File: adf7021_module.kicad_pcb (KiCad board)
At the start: 4 copper layers, 58 x 26 mm, 70 parts, among them J1 Conn_02x10_Counter_Clockwise, J2 Conn_Coaxial, J3 Conn_Coaxial, J4 Conn_02x10_Counter_Clockwise, J5 Conn_Coaxial, J6 Conn_Coaxial, U1 ADF7021, X1 19.68MHz

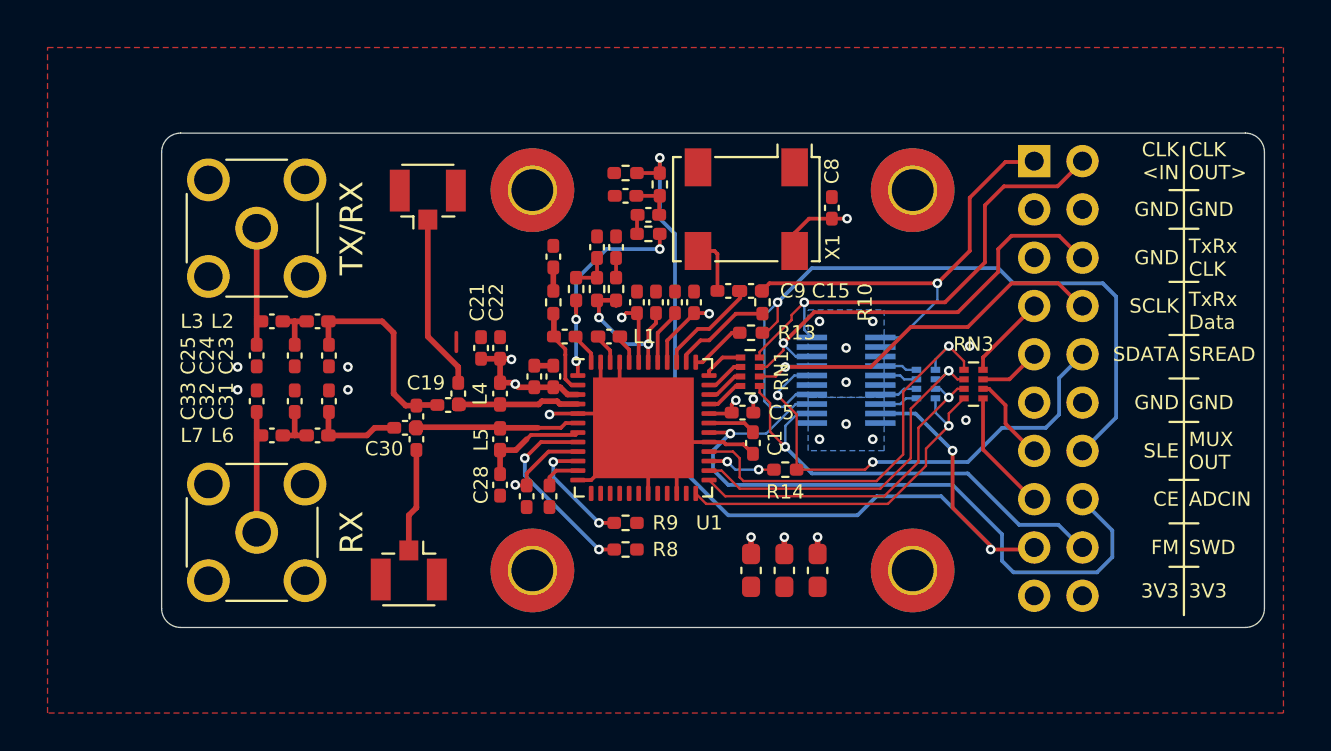
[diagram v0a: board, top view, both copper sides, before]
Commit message: Preliminary via stitching
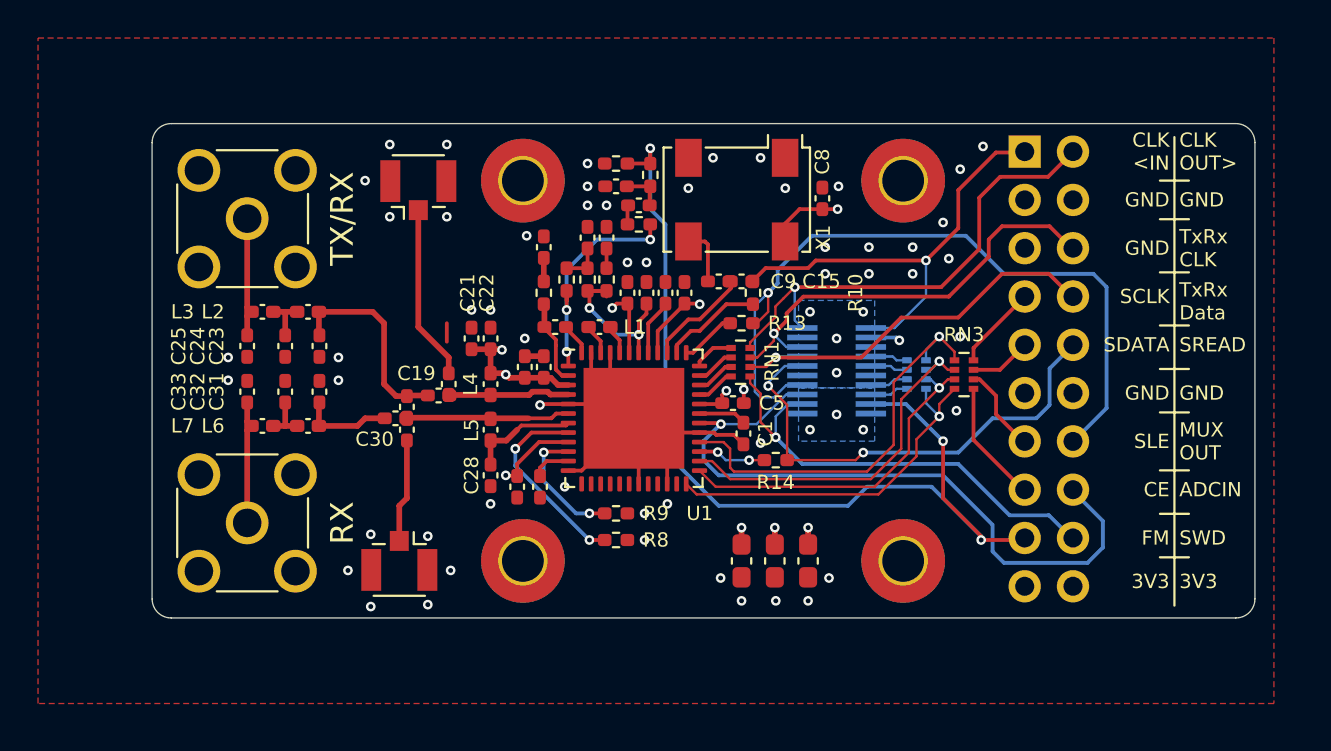
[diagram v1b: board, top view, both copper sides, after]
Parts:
- moved C1 0.71 mm to (136.6, 60.3)
- moved C10 0.71 mm to (131.5, 52.9)
- moved C11 0.71 mm to (129.4, 50.0)
- moved C12 0.71 mm to (128.4, 50.0)
- moved C13 0.71 mm to (126.1, 50.5)
- moved C14 0.71 mm to (132.5, 52.9)
- moved C15 0.71 mm to (136.5, 52.3)
- moved C16 0.71 mm to (131.1, 48.3)
- moved C17 0.71 mm to (129.9, 47.3)
- moved C18 0.71 mm to (121.1, 57.7)
- moved C19 0.71 mm to (120.6, 58.3)
- moved C2 0.71 mm to (133.5, 52.9)
- moved C20 0.71 mm to (124.7, 63.1)
- moved C21 0.71 mm to (122.3, 55.3)
- moved C22 0.71 mm to (123.3, 55.3)
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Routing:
- net GND: track 35.0 -> 36.5 mm, vias 12 -> 60
- net MUXOUT: track 38.5 -> 39.9 mm

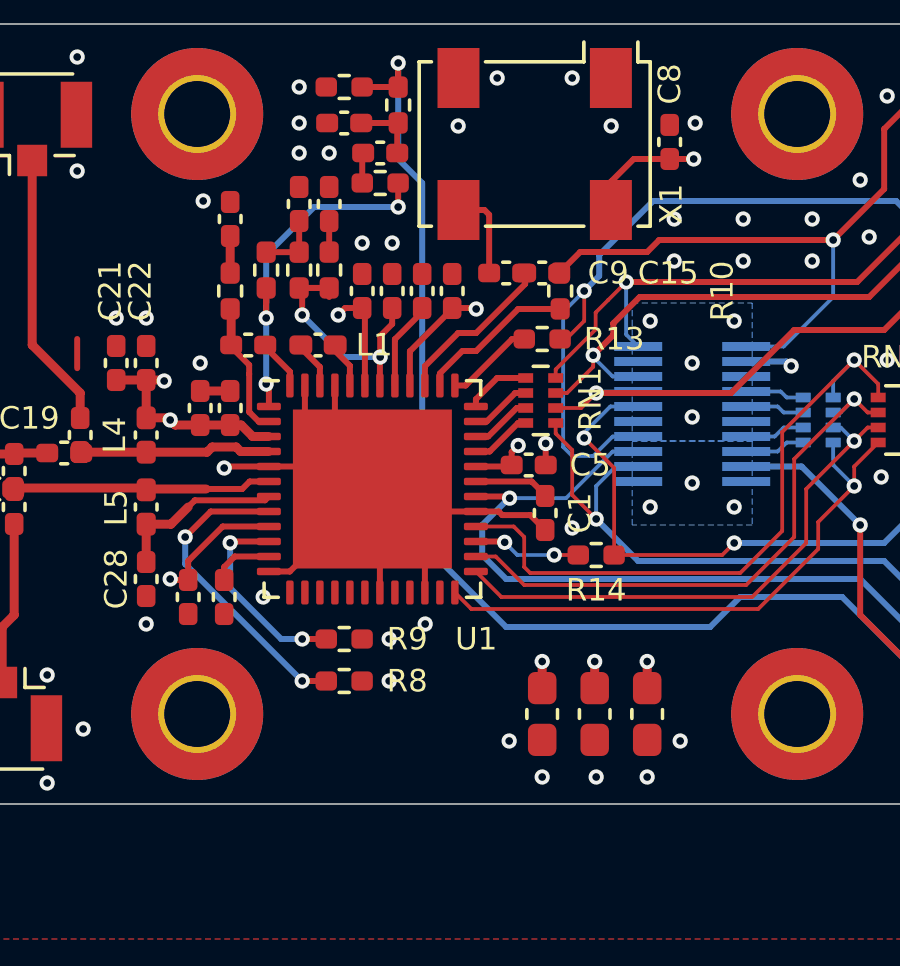
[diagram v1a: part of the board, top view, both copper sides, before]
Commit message: Version silkscreen, via stitching under U1
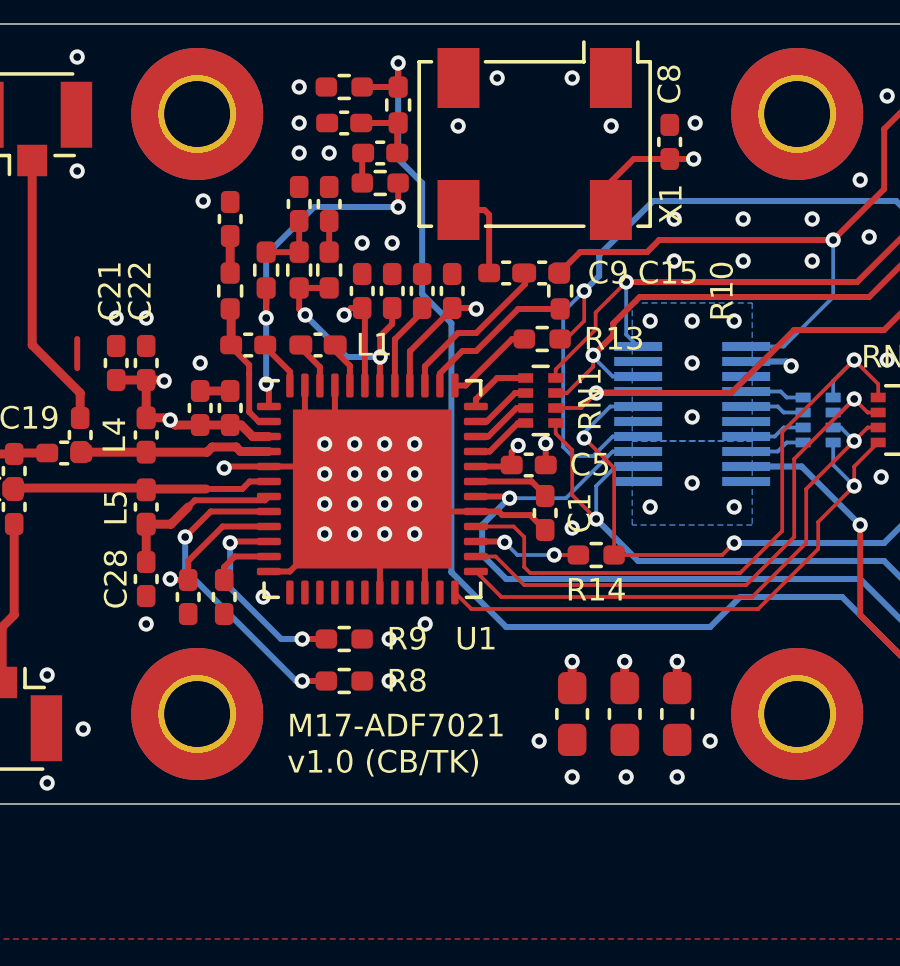
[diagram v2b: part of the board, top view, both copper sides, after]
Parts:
- moved C34 1.00 mm to (141.0, 67.0)
- moved C35 1.00 mm to (139.2, 67.0)
- moved C36 1.00 mm to (137.5, 67.0)
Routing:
- net GND: vias 60 -> 77
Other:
- board text added: "M17-ADF7021 v1.0 (CB/TK)"

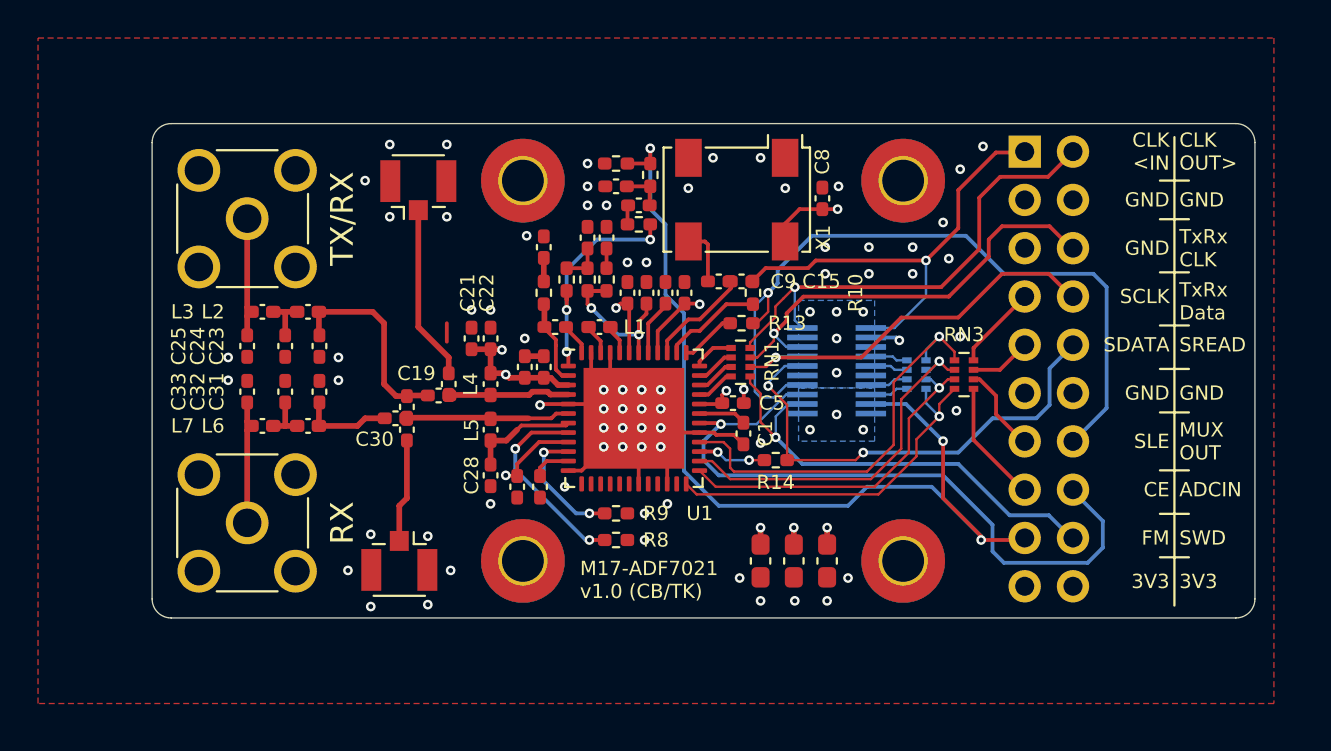
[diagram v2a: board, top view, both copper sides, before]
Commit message: adding shield, moving uFL debug connectors, adding optional SMA clock source input
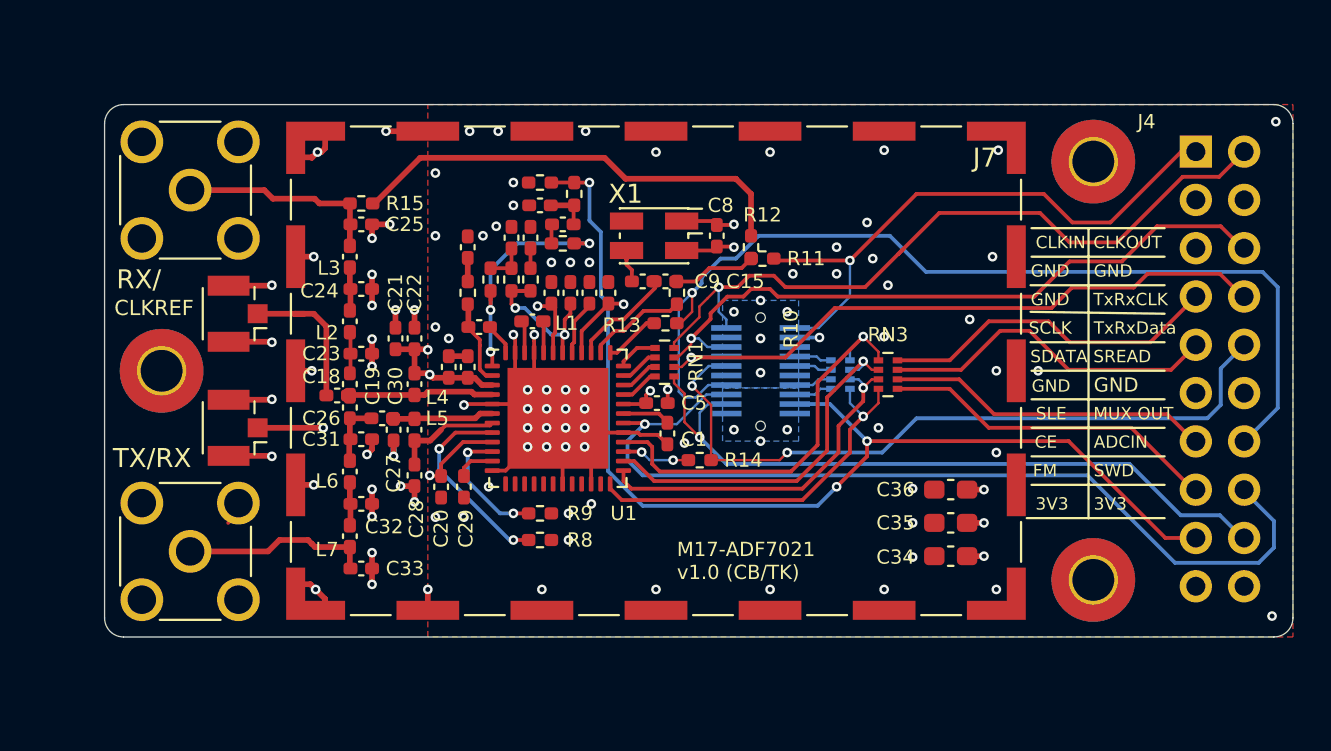
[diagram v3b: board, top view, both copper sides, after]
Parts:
- removed H4: MountingHole_Pad, MountingHole:MountingHole_2.2mm_M2_Pad_TopBottom
- added J7: RFShield_OnePiece, RF_Shielding:Laird_Technologies_BMI-S-205-F_38.10x25.40mm, F.Cu at (132.0, 57.0)
- added R11: 0, Resistor_SMD:R_0402_1005Metric_Pad0.72x0.64mm_HandSolder, F.Cu at (137.6, 51.1)
- added R12: DNP, Resistor_SMD:R_0402_1005Metric_Pad0.72x0.64mm_HandSolder, F.Cu at (137.0, 50.5)
- added R15: DNP, Resistor_SMD:R_0402_1005Metric_Pad0.72x0.64mm_HandSolder, F.Cu at (116.5, 48.2)
- X1: footprint Oscillator:Oscillator_SMD_Fordahl_DFAS2-4Pin_7.3x5.1mm -> Oscillator:Oscillator_SMD_EuroQuartz_XO32-4Pin_3.2x2.5mm_HandSoldering
- moved H3 40.3 mm to (106.0, 57.0)
- moved H1 30.0 mm to (155.0, 46.0)
- moved H2 30.0 mm to (155.0, 68.0)
- moved J5 11.5 mm to (110.0, 54.0), turned to 180 degrees
- moved C33 11.1 mm to (116.5, 67.4), turned to 0 degrees
- moved J6 11.0 mm to (110.0, 60.0), turned to 180 degrees
- moved C36 10.7 mm to (147.5, 63.2), turned to 180 degrees
- moved J4 9.00 mm to (160.4, 45.5)
- moved C25 8.77 mm to (116.5, 49.3), turned to 0 degrees
- moved C35 8.49 mm to (147.5, 65.0), turned to 180 degrees
- moved L7 7.40 mm to (115.9, 65.7), turned to 90 degrees
- moved C32 7.13 mm to (116.5, 64.0), turned to 0 degrees
- moved C34 6.50 mm to (147.5, 66.8), turned to 180 degrees
- moved C18 5.90 mm to (115.2, 58.3), turned to 0 degrees
- moved C8 5.89 mm to (135.2, 49.9)
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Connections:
- C15 pad 1: CLK_IN -> Net-(C15-Pad1)
- C26 pad 1: /RFIN -> /RFOUT
- C26 pad 2: Net-(C19-Pad1) -> Net-(C26-Pad2)
- C30 pad 1: Net-(C30-Pad1) -> Net-(C26-Pad2)
- C31 pad 1: Net-(C30-Pad1) -> Net-(C26-Pad2)
- L6 pad 2: Net-(C30-Pad1) -> Net-(C26-Pad2)
- R10 pad 2: CLK_IN -> Net-(C15-Pad1)
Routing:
- net GND: track 36.5 -> 75.4 mm, vias 77 -> 101
- net CLK_SMA: track 0.00 -> 23.9 mm
- net Net-(J4-Pad9): track 3.19 -> 17.9 mm
- net CLKOUT: track 25.6 -> 39.2 mm
- net Net-(J4-Pad7): track 4.41 -> 17.9 mm
- net TxRxData: track 20.9 -> 34.4 mm
- net SWD: track 24.3 -> 37.5 mm
- net SREAD: track 25.3 -> 38.3 mm
- net TxRxCLK: track 23.1 -> 36.0 mm
- net MUXOUT: track 39.9 -> 52.7 mm
- net Net-(J4-Pad13): track 4.60 -> 17.0 mm
- net ADCIN: track 36.5 -> 48.7 mm
- net Net-(J4-Pad15): track 6.45 -> 17.9 mm
- net Net-(C19-Pad1): track 10.7 -> 2.19 mm
- net CLK_IN: track 23.8 -> 31.4 mm
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- added copper zone on In2.Cu, net Net-(C27-Pad2)
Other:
- board size 58 x 26 mm -> 62.5 x 28 mm
- board text added: "CLKIN"
- board text added: "CLKOUT"
- board text added: "CLKREF"
- board text added: "L1 12mil / 0.3mm L3 ~~2mm trace should be 50Ωish"
- board text added: "RX/"
- board text added: "TxRxCLK"
- board text added: "TxRxData"
- board text removed: "12mil / 0.3mm trace should be 50Ωish"
- board text removed: "CLK <IN"
- board text removed: "CLK OUT>"
- board text removed: "RX"
- board text removed: "TxRx CLK"
- board text removed: "TxRx Data"

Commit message: adding VFO pin
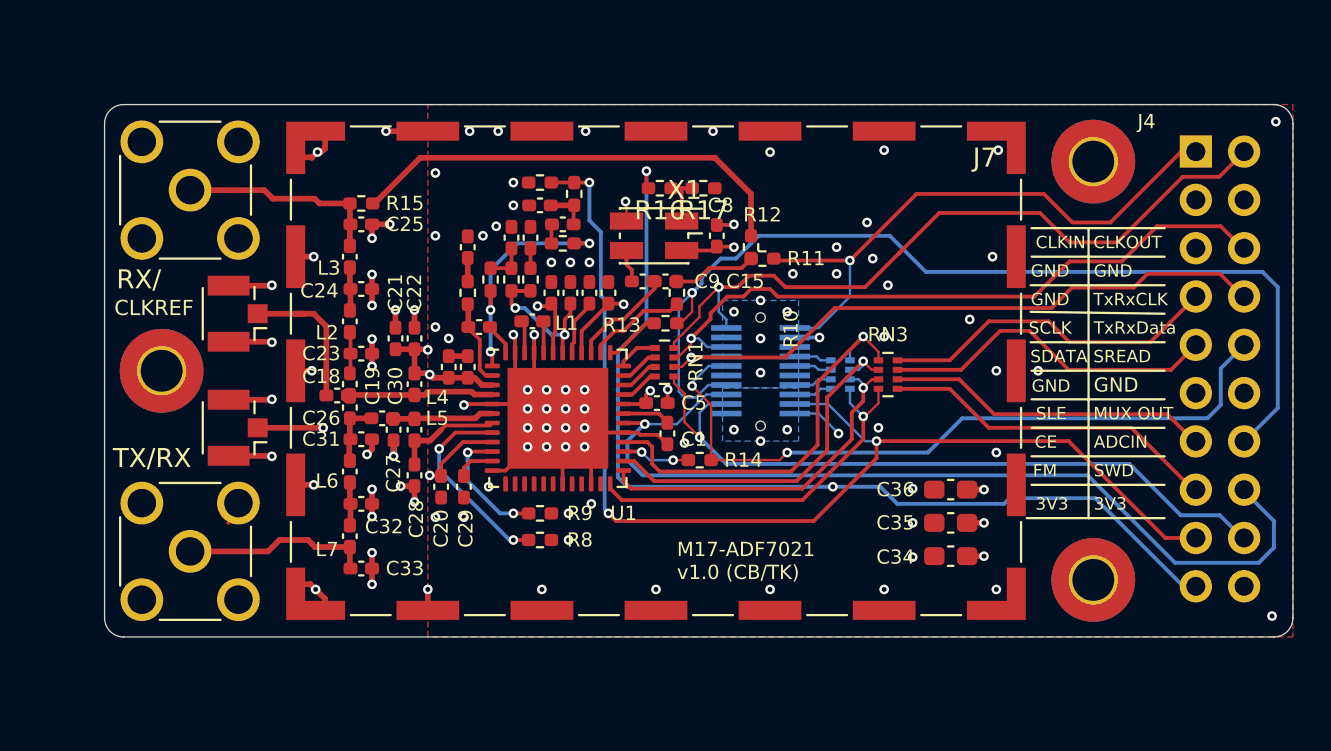
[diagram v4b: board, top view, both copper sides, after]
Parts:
- added R16: DNP, Resistor_SMD:R_0402_1005Metric_Pad0.72x0.64mm_HandSolder, F.Cu at (132.2, 47.4)
- added R17: 0R, Resistor_SMD:R_0402_1005Metric_Pad0.72x0.64mm_HandSolder, F.Cu at (134.5, 47.4)
- J1: value Conn_02x10_Counter_Clockwise -> Conn_Board2Board
- J4: value Conn_02x10_Counter_Clockwise -> Conn_goldpin
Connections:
- J1 pad 10: +3V3 -> VCO_MOD
- J1 pad 2: GND -> +3V3
- J4 pad 19: +3V3 -> VCO_MOD
- J4 pad 3: GND -> +3V3
- X1 pad 1: GND -> Net-(R16-Pad1)
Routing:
- net VCO_MOD: track 0.00 -> 57.2 mm, vias 0 -> 3
- net Net-(R16-Pad1): track 0.00 -> 2.85 mm
- net FM_MOD: track 57.9 -> 60.4 mm
- net GND: track 75.4 -> 73.5 mm
- net +3V3: track 26.8 -> 28.1 mm, vias 13 -> 14
